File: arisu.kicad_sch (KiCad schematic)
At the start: 2 parts, among them J7 Conn_01x03_Male, J8 Conn_01x03_Female

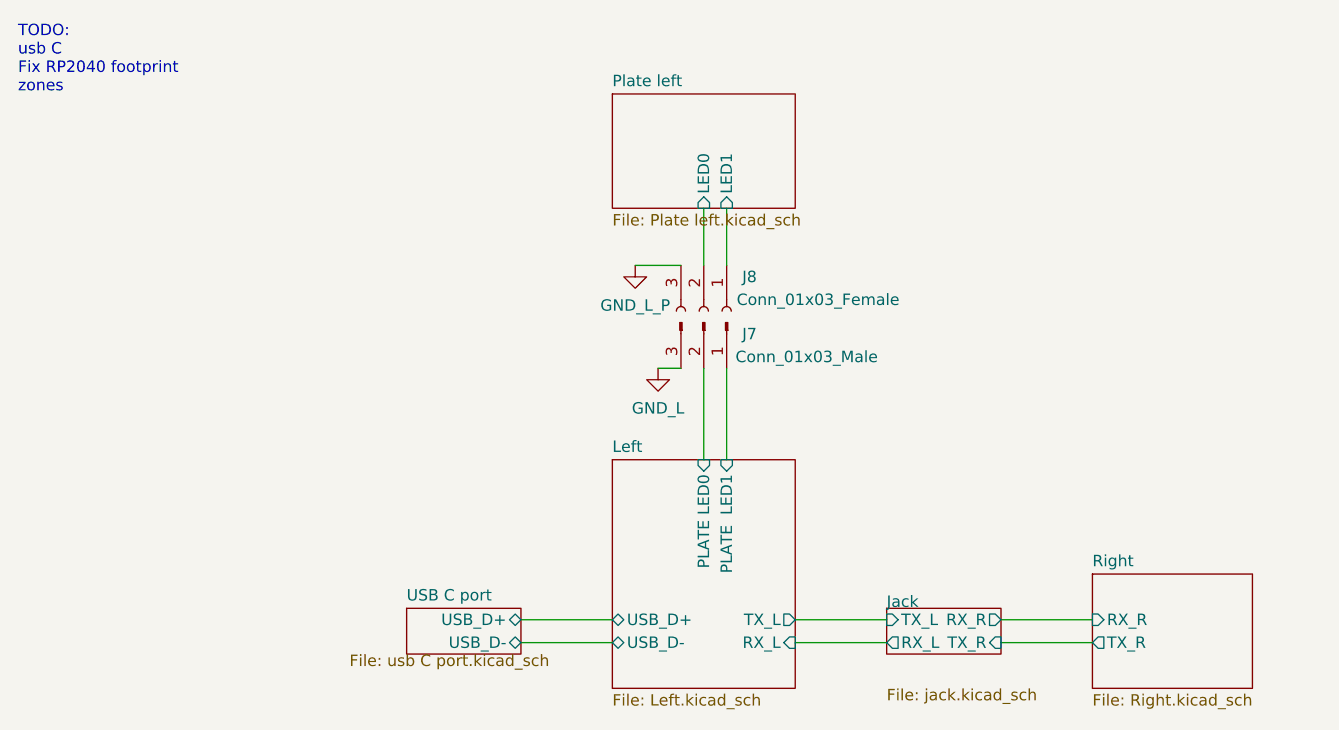
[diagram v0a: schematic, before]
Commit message: Left side case created in blender
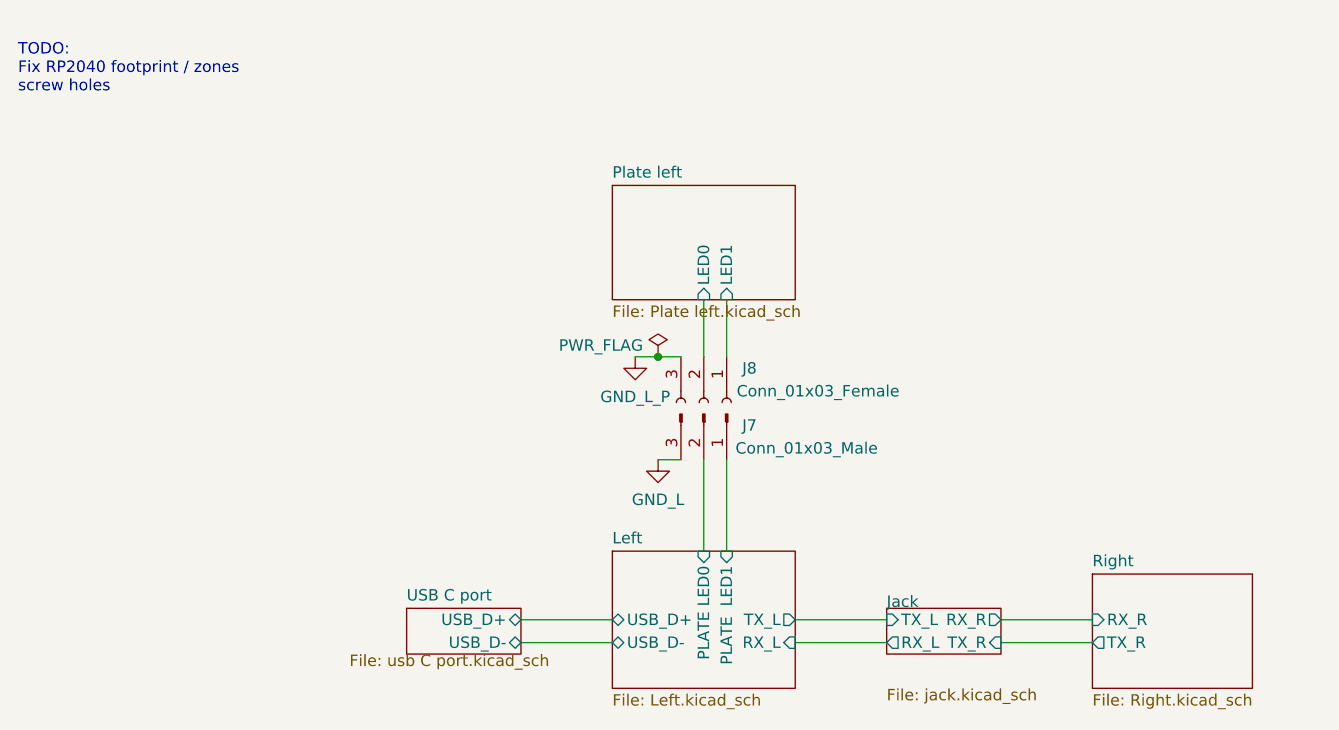
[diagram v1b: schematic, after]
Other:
- note added: "TODO: Fix RP2040 footprint / zones screw holes"
- note removed: "TODO: usb C Fix RP2040 footprint zones"
- moved on the sheet: J7, J8

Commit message: temp commit, squash with next
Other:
- note added: "TODO: screw holes"
- note removed: "TODO: Fix RP2040 footprint / zones screw holes"
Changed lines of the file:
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@@
     (stroke (width 0) (type default) (color 0 0 0 0))
   )
-  (text "TODO:\nFix RP2040 footprint / zones\nscrew holes\n" (at 15.24 30.48 0)
+  (text "TODO:\nscrew holes\n" (at 15.24 30.48 0)
     (effects (font (size 1.27 1.27)) (justify left bottom))
   )

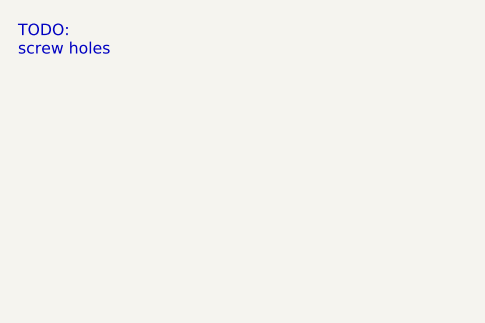
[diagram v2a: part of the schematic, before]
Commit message: Fix left shift footprint, add stabilizer cutouts back in
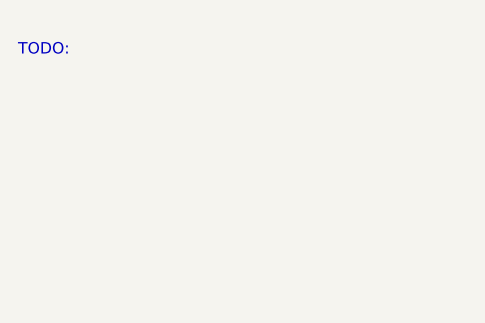
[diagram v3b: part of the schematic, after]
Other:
- note added: "TODO:"
- note removed: "TODO: screw holes"
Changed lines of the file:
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@@
     (stroke (width 0) (type default) (color 0 0 0 0))
   )
-  (text "TODO:\nscrew holes\n" (at 15.24 30.48 0)
+  (text "TODO:\n" (at 15.24 30.48 0)
     (effects (font (size 1.27 1.27)) (justify left bottom))
   )
@@
     )
     (path "/769dae23-5223-4917-97f1-926f10044dd4/39d8773e-a4e7-456f-b68b-dabcfc0d2cf5/00000000-0000-0000-0000-00005c520f5d"
-      (reference "SW7") (unit 1) (value "~") (footprint "MX_Switch:SW_Cherry_MX_2.00u_PCB_Socket_ReversedStabilizers")
+      (reference "SW7") (unit 1) (value "~") (footprint "MX_Switch:SW_Cherry_MX_2.00u_PCB_Socket")
     )
     (path "/769dae23-5223-4917-97f1-926f10044dd4/39d8773e-a4e7-456f-b68b-dabcfc0d2cf5/21ac8e93-ff76-4720-966b-42dcd13d6562"
